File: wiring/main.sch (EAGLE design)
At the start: 48 parts, among them IC1 attiny 2313A, J1 J7MM, J11 J7MM, J2 J5MM, J3 J10MM, J4 J7MM, J5 J5MM, J6 J5MM, Q1 12MHz, X1 USB-B

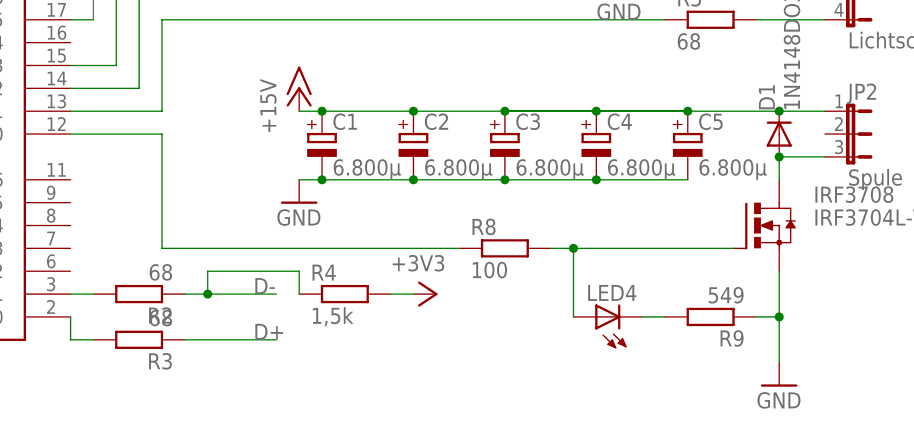
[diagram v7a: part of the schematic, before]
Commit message: wiring schaltazeige led Widerstand geändert
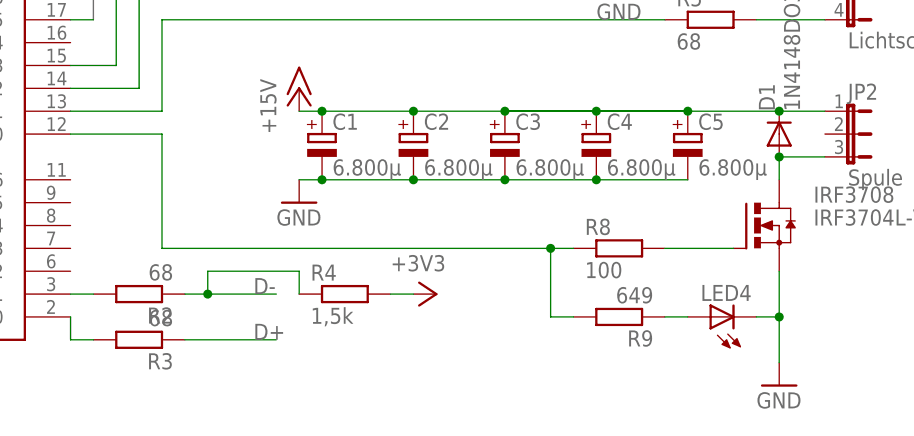
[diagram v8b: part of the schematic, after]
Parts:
- R9: value 549 -> 649
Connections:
- removed net N$6: LED4.C, R9.2
- new net N$7: LED4.A, R9.1
- net GND: now also LED4.C; no longer R9.1
- net N$2: no longer LED4.A
- net PB0: now also R9.2
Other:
- moved on the sheet: LED4, R8, R9
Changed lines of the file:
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@@
 <grid distance="0.1" unitdist="inch" unit="inch" style="lines" multiple="1" display="no" altdistance="0.01" altunitdist="inch" altunit="inch"/>
 <layers>
-<layer number="1" name="Top" color="4" fill="1" visible="yes" active="no"/>
-<layer number="16" name="Bottom" color="1" fill="1" visible="yes" active="no"/>
-<layer number="17" name="Pads" color="2" fill="1" visible="yes" active="no"/>
-<layer number="18" name="Vias" color="2" fill="1" visible="yes" active="no"/>
-<layer number="19" name="Unrouted" color="6" fill="1" visible="yes" active="no"/>
-<layer number="20" name="Dimension" color="15" fill="1" visible="yes" active="no"/>
-<layer number="21" name="tPlace" color="7" fill="1" visible="yes" active="no"/>
-<layer number="22" name="bPlace" color="7" fill="1" visible="yes" active="no"/>
-<layer number="23" name="tOrigins" color="15" fill="1" visible="yes" active="no"/>
-<layer number="24" name="bOrigins" color="15" fill="1" visible="yes" active="no"/>
-<layer number="25" name="tNames" color="7" fill="1" visible="yes" active="no"/>
-<layer number="26" name="bNames" color="7" fill="1" visible="yes" active="no"/>
-<layer number="27" name="tValues" color="7" fill="1" visible="yes" active="no"/>
-<layer number="28" name="bValues" color="7" fill="1" visible="yes" active="no"/>
+<layer number="1" name="Top" color="4" fill="1" visible="no" active="no"/>
+<layer number="16" name="Bottom" color="1" fill="1" visible="no" active="no"/>
+<layer number="17" name="Pads" color="2" fill="1" visible="no" active="no"/>
+<layer number="18" name="Vias" color="2" fill="1" visible="no" active="no"/>
+<layer number="19" name="Unrouted" color="6" fill="1" visible="no" active="no"/>
+<layer number="20" name="Dimension" color="15" fill="1" visible="no" active="no"/>
+<layer number="21" name="tPlace" color="7" fill="1" visible="no" active="no"/>
+<layer number="22" name="bPlace" color="7" fill="1" visible="no" active="no"/>
+<layer number="23" name="tOrigins" color="15" fill="1" visible="no" active="no"/>
+<layer number="24" name="bOrigins" color="15" fill="1" visible="no" active="no"/>
+<layer number="25" name="tNames" color="7" fill="1" visible="no" active="no"/>
+<layer number="26" name="bNames" color="7" fill="1" visible="no" active="no"/>
+<layer number="27" name="tValues" color="7" fill="1" visible="no" active="no"/>
+<layer number="28" name="bValues" color="7" fill="1" visible="no" active="no"/>
 <layer number="29" name="tStop" color="7" fill="3" visible="no" active="no"/>
 <layer number="30" name="bStop" color="7" fill="6" visible="no" active="no"/>
@@
 <layer number="35" name="tGlue" color="7" fill="4" visible="no" active="no"/>
 <layer number="36" name="bGlue" color="7" fill="5" visible="no" active="no"/>
-<layer number="37" name="tTest" color="7" fill="1" visible="yes" active="no"/>
-<layer number="38" name="bTest" color="7" fill="1" visible="yes" active="no"/>
+<layer number="37" name="tTest" color="7" fill="1" visible="no" active="no"/>
+<layer number="38" name="bTest" color="7" fill="1" visible="no" active="no"/>
 <layer number="39" name="tKeepout" color="4" fill="11" visible="no" active="no"/>
 <layer number="40" name="bKeepout" color="1" fill="11" visible="no" active="no"/>
@@
 <layer number="44" name="Drills" color="7" fill="1" visible="no" active="no"/>
 <layer number="45" name="Holes" color="7" fill="1" visible="no" active="no"/>
-<layer number="46" name="Milling" color="3" fill="1" visible="yes" active="no"/>
-<layer number="47" name="Measures" color="7" fill="1" visible="yes" active="no"/>
-<layer number="48" name="Document" color="7" fill="1" visible="yes" active="no"/>
-<layer number="49" name="Reference" color="7" fill="1" visible="yes" active="no"/>
-<layer number="50" name="dxf" color="7" fill="1" visible="yes" active="no"/>
-<layer number="51" name="tDocu" color="7" fill="1" visible="yes" active="no"/>
-<layer number="52" name="bDocu" color="7" fill="1" visible="yes" active="no"/>
+<layer number="46" name="Milling" color="3" fill="1" visible="no" active="no"/>
+<layer number="47" name="Measures" color="7" fill="1" visible="no" active="no"/>
+<layer number="48" name="Document" color="7" fill="1" visible="no" active="no"/>
+<layer number="49" name="Reference" color="7" fill="1" visible="no" active="no"/>
+<layer number="50" name="dxf" color="7" fill="1" visible="no" active="no"/>
+<layer number="51" name="tDocu" color="7" fill="1" visible="no" active="no"/>
+<layer number="52" name="bDocu" color="7" fill="1" visible="no" active="no"/>
 <layer number="91" name="Nets" color="2" fill="1" visible="yes" active="yes"/>
 <layer number="92" name="Busses" color="1" fill="1" visible="yes" active="yes"/>
@@
 <part name="D1" library="diode" deviceset="1N4148" device="DO35-7"/>
 <part name="IRF3708" library="transistor-power" deviceset="IRF3704" device="L-V"/>
-<part name="R9" library="rcl" deviceset="R-EU_" device="0207/10" value="549"/>
+<part name="R9" library="rcl" deviceset="R-EU_" device="0207/10" value="649"/>
 <part name="C8" library="resistor" deviceset="CPOL-EU" device="E2.5-7" value="220µ"/>
 <part name="P+5" library="supply1" deviceset="+15V" device=""/>
@@
 <instance part="C7" gate="G$1" x="17.78" y="109.22"/>
 <instance part="C10" gate="G$1" x="-12.7" y="33.02"/>
-<instance part="R8" gate="G$1" x="91.44" y="22.86"/>
+<instance part="R8" gate="G$1" x="104.14" y="22.86"/>
 <instance part="R1" gate="G$1" x="-5.08" y="53.34"/>
 <instance part="C13" gate="G$1" x="-5.08" y="40.64" rot="R270"/>
@@
 <instance part="D1" gate="G$1" x="121.92" y="35.56" rot="R90"/>
 <instance part="IRF3708" gate="G$1" x="119.38" y="25.4"/>
-<instance part="R9" gate="G$1" x="114.3" y="15.24" rot="R180"/>
+<instance part="R9" gate="G$1" x="104.14" y="15.24" rot="R180"/>
 <instance part="C8" gate="G$1" x="27.94" y="109.22"/>
 <instance part="P+5" gate="1" x="86.36" y="111.76" rot="R270"/>
@@
 <instance part="P+11" gate="1" x="162.56" y="119.38"/>
 <instance part="P+12" gate="1" x="7.62" y="119.38"/>
-<instance part="LED4" gate="G$1" x="101.6" y="15.24" rot="R90"/>
+<instance part="LED4" gate="G$1" x="114.3" y="15.24" rot="R90"/>
 </instances>
 <busses>
@@
 <pinref part="R8" gate="G$1" pin="2"/>
 <pinref part="IRF3708" gate="G$1" pin="G"/>
-<wire x1="96.52" y1="22.86" x2="99.06" y2="22.86" width="0.1524" layer="91"/>
-<pinref part="LED4" gate="G$1" pin="A"/>
-<wire x1="99.06" y1="22.86" x2="116.84" y2="22.86" width="0.1524" layer="91"/>
-<wire x1="99.06" y1="15.24" x2="99.06" y2="22.86" width="0.1524" layer="91"/>
-<junction x="99.06" y="22.86"/>
+<wire x1="109.22" y1="22.86" x2="116.84" y2="22.86" width="0.1524" layer="91"/>
 </segment>
 </net>
@@
 <segment>
 <pinref part="R8" gate="G$1" pin="1"/>
-<wire x1="86.36" y1="22.86" x2="53.34" y2="22.86" width="0.1524" layer="91"/>
 <pinref part="IC1" gate="G$1" pin="(AIN0)PB0"/>
+<wire x1="99.06" y1="22.86" x2="96.52" y2="22.86" width="0.1524" layer="91"/>
+<wire x1="96.52" y1="22.86" x2="53.34" y2="22.86" width="0.1524" layer="91"/>
 <wire x1="53.34" y1="22.86" x2="53.34" y2="35.56" width="0.1524" layer="91"/>
 <wire x1="53.34" y1="35.56" x2="43.18" y2="35.56" width="0.1524" layer="91"/>
+<pinref part="R9" gate="G$1" pin="2"/>
+<wire x1="99.06" y1="15.24" x2="96.52" y2="15.24" width="0.1524" layer="91"/>
+<wire x1="96.52" y1="15.24" x2="96.52" y2="22.86" width="0.1524" layer="91"/>
+<junction x="96.52" y="22.86"/>
 </segment>
 </net>
@@
 <pinref part="GND6" gate="1" pin="GND"/>
 <pinref part="IRF3708" gate="G$1" pin="S"/>
-<pinref part="R9" gate="G$1" pin="1"/>
 <wire x1="121.92" y1="10.16" x2="121.92" y2="15.24" width="0.1524" layer="91"/>
+<pinref part="LED4" gate="G$1" pin="C"/>
 <wire x1="121.92" y1="15.24" x2="121.92" y2="20.32" width="0.1524" layer="91"/>
 <wire x1="119.38" y1="15.24" x2="121.92" y2="15.24" width="0.1524" layer="91"/>
@@
 </segment>
 </net>
-<net name="N$6" class="0">
-<segment>
-<pinref part="R9" gate="G$1" pin="2"/>
-<pinref part="LED4" gate="G$1" pin="C"/>
-<wire x1="106.68" y1="15.24" x2="109.22" y2="15.24" width="0.1524" layer="91"/>
-</segment>
-</net>
+<net name="N$7" class="0">
+<segment>
+<pinref part="R9" gate="G$1" pin="1"/>
+<pinref part="LED4" gate="G$1" pin="A"/>
+<wire x1="109.22" y1="15.24" x2="111.76" y2="15.24" width="0.1524" layer="91"/>
+</segment>
+</net>
